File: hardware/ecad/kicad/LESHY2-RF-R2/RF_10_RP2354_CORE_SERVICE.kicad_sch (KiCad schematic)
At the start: 48 parts, among them J3 Samtec FTSH-105-01-L-DV-K-P-TR, J4 GCT USB4105-GF-A, SW1 Alps Alpine SKRTLAE010, SW2 Alps Alpine SKRTLAE010, U22 SC1512-A4, U23 Texas Instruments TPD4E05U06D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, U24 Texas Instruments TPD2EUSB30A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, U25 onsemi FSUSB42MUX, Y1 Abracon ABM8-272-T3

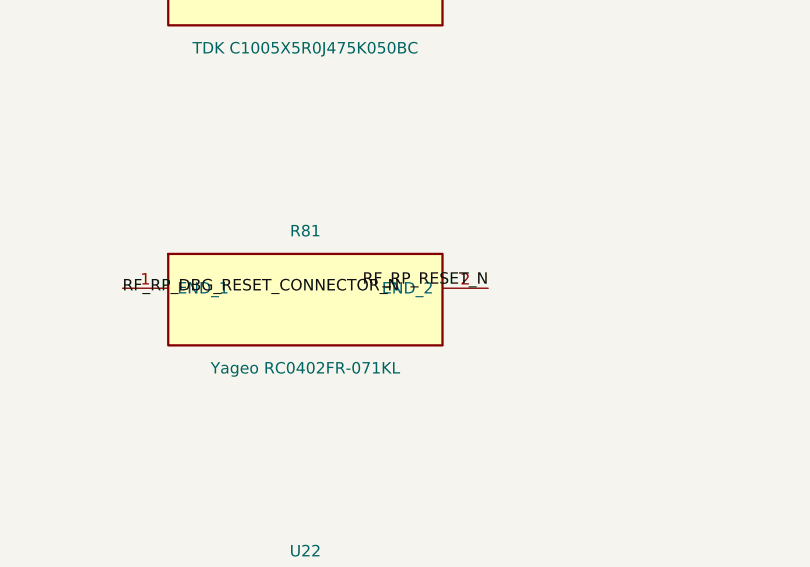
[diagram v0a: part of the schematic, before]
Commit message: Connect RF emergency reset to active RP reset net
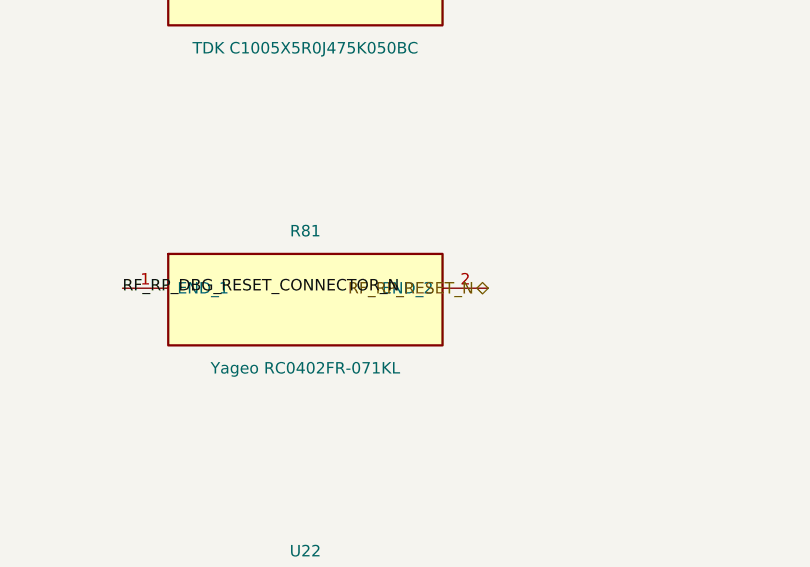
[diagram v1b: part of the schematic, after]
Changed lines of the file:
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@@
 		(effects (font (size 1.27 1.27)))
 	)
-	(label "RF_RP_RESET_N"
+	(hierarchical_label "RF_RP_RESET_N"
+		(shape bidirectional)
 		(at 716.28 121.92 180)
 		(effects (font (size 1.27 1.27)) (justify right bottom))

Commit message: Complete current R2 schematic and sourcing revalidation
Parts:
- renumbered C95 to C100, C96 to C101, C97 to C102, C98 to C103, C99 to C104, C100 to C105, C80 to C85, C81 to C86, C82 to C87, C83 to C88, C84 to C89, C85 to C90, C86 to C91, C87 to C92, C88 to C93, C89 to C94, C90 to C95, C91 to C96, C92 to C97, C93 to C98, C94 to C99, L5 to L4, R74 to R75, R75 to R76, R76 to R77, R77 to R78, R78 to R79, R79 to R80, R80 to R81, R81 to R82, R82 to R83, R83 to R84, R84 to R85, R85 to R86, R86 to R87, R87 to R88, R88 to R89, R89 to R90, R90 to R91, U22 to U23, U23 to U24, U24 to U25, U25 to U26
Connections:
- net CAP_PIN10_BUSY_OR_NFC_CS_N renamed CAP_PIN10_HOST

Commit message: Bind H6 RF and USB routing geometry
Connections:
- net RF_RP_SERVICE_USB_DM_CONNECTOR renamed RF_RP_SERVICE_USB_CONNECTOR_N
- net RF_RP_SERVICE_USB_DM_SWITCHED renamed RF_RP_SERVICE_USB_SWITCHED_N
- net RF_RP_SERVICE_USB_DP_CONNECTOR renamed RF_RP_SERVICE_USB_CONNECTOR_P
- net RF_RP_SERVICE_USB_DP_SWITCHED renamed RF_RP_SERVICE_USB_SWITCHED_P
- net RF_RP_USB_DM renamed RF_RP_USB_N
- net RF_RP_USB_DP renamed RF_RP_USB_P
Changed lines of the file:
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@@
 		(effects (font (size 1.27 1.27)))
 	)
-	(label "RF_RP_SERVICE_USB_DP_CONNECTOR"
+	(label "RF_RP_SERVICE_USB_CONNECTOR_P"
 		(at 949.96 91.44 0)
 		(effects (font (size 1.27 1.27)))
 	)
-	(label "RF_RP_SERVICE_USB_DM_CONNECTOR"
+	(label "RF_RP_SERVICE_USB_CONNECTOR_N"
 		(at 949.96 93.98 0)
 		(effects (font (size 1.27 1.27)))
@@
 		(effects (font (size 1.27 1.27)) (justify right bottom))
 	)
-	(label "RF_RP_SERVICE_USB_DP_CONNECTOR"
+	(label "RF_RP_SERVICE_USB_CONNECTOR_P"
 		(at 990.60 88.90 180)
 		(effects (font (size 1.27 1.27)) (justify right bottom))
 	)
-	(label "RF_RP_SERVICE_USB_DM_CONNECTOR"
+	(label "RF_RP_SERVICE_USB_CONNECTOR_N"
 		(at 990.60 91.44 180)
 		(effects (font (size 1.27 1.27)) (justify right bottom))
@@
 		)
 	)
-	(label "RF_RP_SERVICE_USB_DM_SWITCHED"
+	(label "RF_RP_SERVICE_USB_SWITCHED_N"
 		(at 35.56 157.48 0)
 		(effects (font (size 1.27 1.27)))
 	)
-	(label "RF_RP_USB_DM"
+	(label "RF_RP_USB_N"
 		(at 76.20 157.48 180)
 		(effects (font (size 1.27 1.27)) (justify right bottom))
@@
 		)
 	)
-	(label "RF_RP_SERVICE_USB_DP_SWITCHED"
+	(label "RF_RP_SERVICE_USB_SWITCHED_P"
 		(at 127.00 157.48 0)
 		(effects (font (size 1.27 1.27)))
 	)
-	(label "RF_RP_USB_DP"
+	(label "RF_RP_USB_P"
 		(at 167.64 157.48 180)
 		(effects (font (size 1.27 1.27)) (justify right bottom))
@@
 		(effects (font (size 1.27 1.27)) (justify right bottom))
 	)
-	(label "RF_RP_USB_DM"
+	(label "RF_RP_USB_N"
 		(at 716.28 215.90 180)
 		(effects (font (size 1.27 1.27)) (justify right bottom))
 	)
-	(label "RF_RP_USB_DP"
+	(label "RF_RP_USB_P"
 		(at 716.28 218.44 180)
 		(effects (font (size 1.27 1.27)) (justify right bottom))
@@
 		)
 	)
-	(label "RF_RP_SERVICE_USB_DP_CONNECTOR"
+	(label "RF_RP_SERVICE_USB_CONNECTOR_P"
 		(at 1041.40 157.48 0)
 		(effects (font (size 1.27 1.27)))
 	)
-	(label "RF_RP_SERVICE_USB_DM_CONNECTOR"
+	(label "RF_RP_SERVICE_USB_CONNECTOR_N"
 		(at 1041.40 160.02 0)
 		(effects (font (size 1.27 1.27)))
@@
 		(effects (font (size 1.27 1.27)))
 	)
-	(label "RF_RP_SERVICE_USB_DP_CONNECTOR"
+	(label "RF_RP_SERVICE_USB_CONNECTOR_P"
 		(at 858.52 162.56 0)
 		(effects (font (size 1.27 1.27)))
 	)
-	(label "RF_RP_SERVICE_USB_DM_CONNECTOR"
+	(label "RF_RP_SERVICE_USB_CONNECTOR_N"
 		(at 858.52 165.10 0)
 		(effects (font (size 1.27 1.27)))
@@
 		(effects (font (size 1.27 1.27)))
 	)
-	(label "RF_RP_SERVICE_USB_DM_SWITCHED"
+	(label "RF_RP_SERVICE_USB_SWITCHED_N"
 		(at 899.16 157.48 180)
 		(effects (font (size 1.27 1.27)) (justify right bottom))
 	)
-	(label "RF_RP_SERVICE_USB_DP_SWITCHED"
+	(label "RF_RP_SERVICE_USB_SWITCHED_P"
 		(at 899.16 160.02 180)
 		(effects (font (size 1.27 1.27)) (justify right bottom))

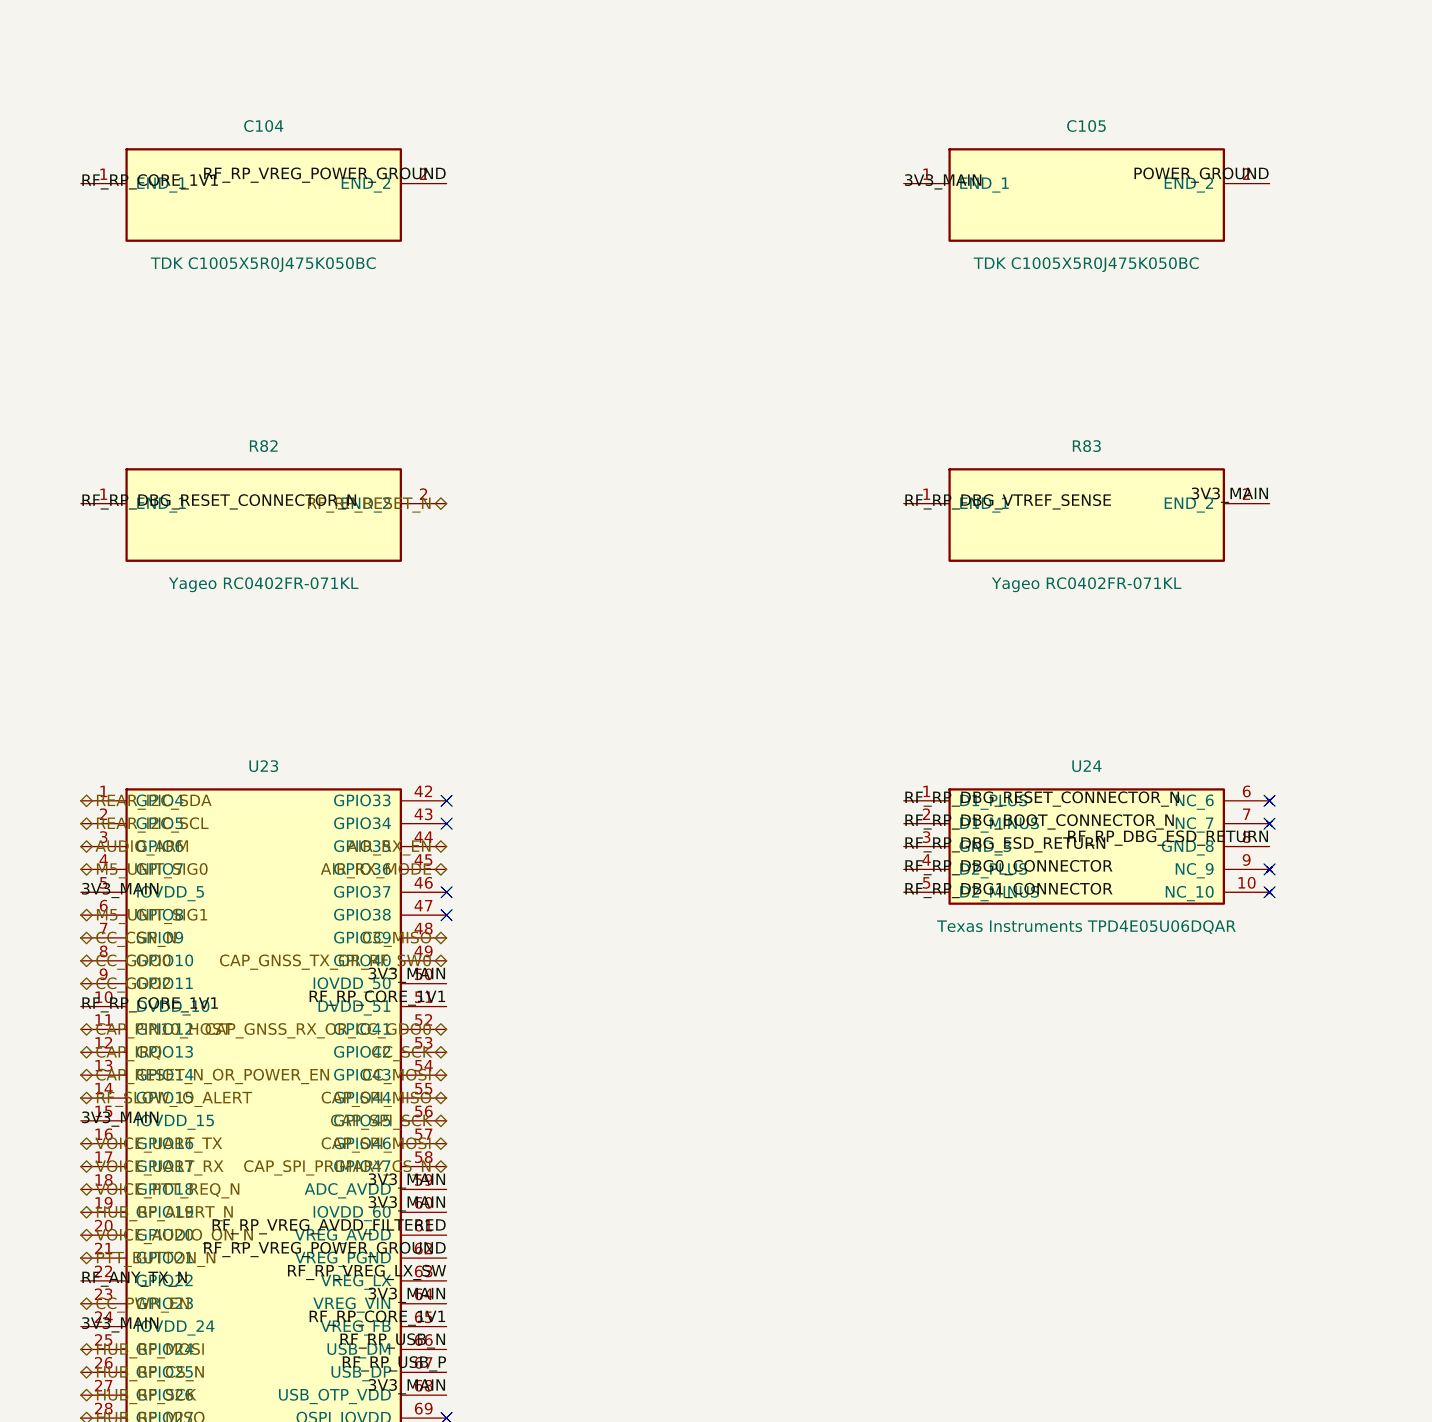
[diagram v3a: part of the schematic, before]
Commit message: Canonicalize physical ground anchors
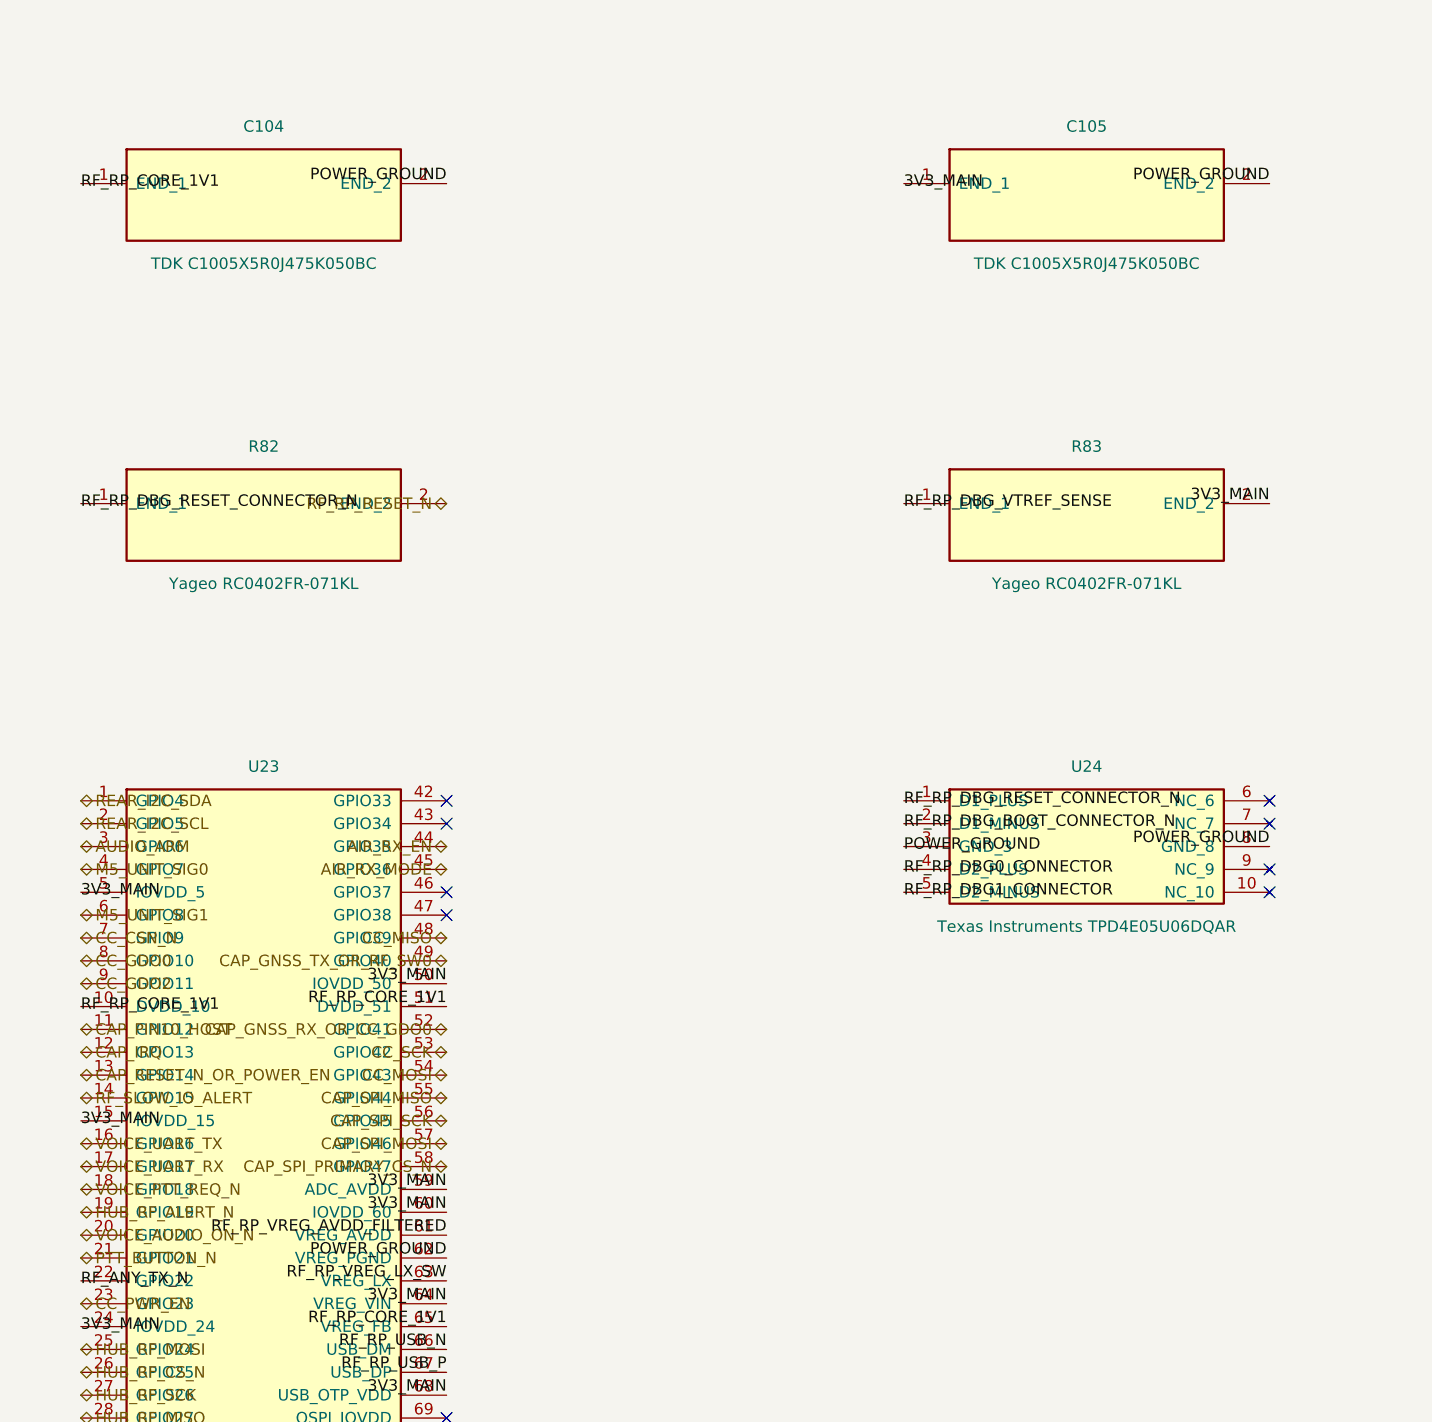
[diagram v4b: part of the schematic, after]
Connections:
- net RF_RP_DBG_ESD_RETURN is gone; now on net POWER_GROUND: U24.3 (GND_3), U24.8 (GND_8)
- net RF_RP_VREG_POWER_GROUND is gone; now on net POWER_GROUND: C104.2 (END_2), U23.62 (VREG_PGND)
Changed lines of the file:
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@@
 		(effects (font (size 1.27 1.27)))
 	)
-	(label "RF_RP_VREG_POWER_GROUND"
+	(label "POWER_GROUND"
 		(at 716.28 86.36 180)
 		(effects (font (size 1.27 1.27)) (justify right bottom))
@@
 		(effects (font (size 1.27 1.27)) (justify right bottom))
 	)
-	(label "RF_RP_VREG_POWER_GROUND"
+	(label "POWER_GROUND"
 		(at 716.28 205.74 180)
 		(effects (font (size 1.27 1.27)) (justify right bottom))
@@
 		(effects (font (size 1.27 1.27)))
 	)
-	(label "RF_RP_DBG_ESD_RETURN"
+	(label "POWER_GROUND"
 		(at 767.08 160.02 0)
 		(effects (font (size 1.27 1.27)))
@@
 	(no_connect (at 807.72 157.48)
 	)
-	(label "RF_RP_DBG_ESD_RETURN"
+	(label "POWER_GROUND"
 		(at 807.72 160.02 180)
 		(effects (font (size 1.27 1.27)) (justify right bottom))

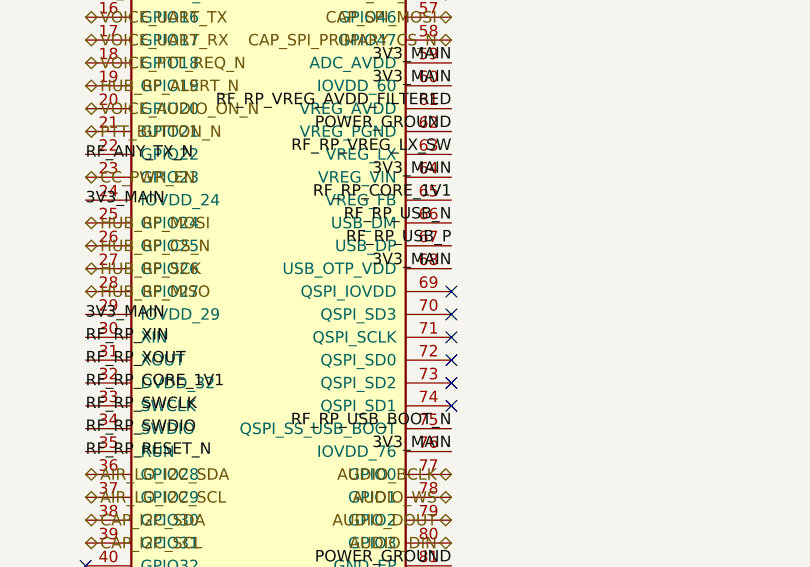
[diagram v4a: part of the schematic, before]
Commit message: Fix exact pin maps and RP flash power; add typed electrical review
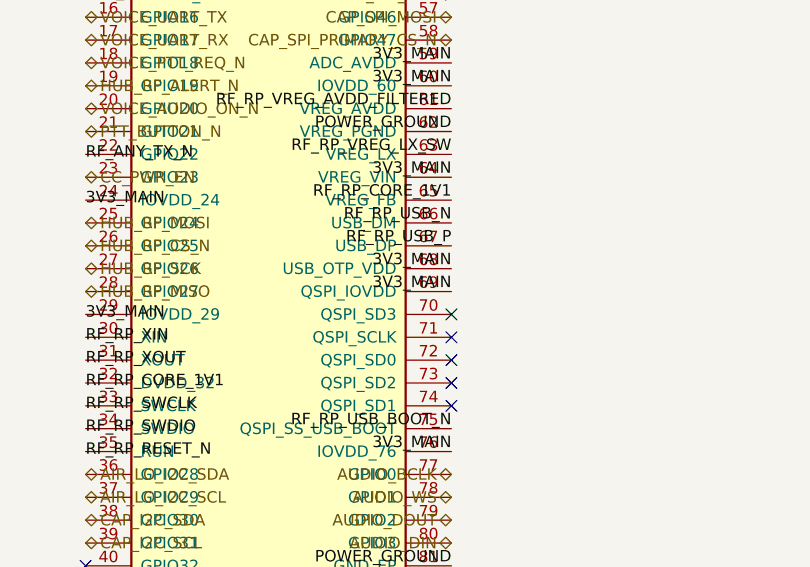
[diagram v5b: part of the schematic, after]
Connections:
- net 3V3_MAIN: now also U23.69 (QSPI_IOVDD)
- no-connect marks 19 -> 18
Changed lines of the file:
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@@
 		(effects (font (size 1.27 1.27)) (justify right bottom))
 	)
-	(no_connect (at 716.28 223.52)
+	(label "3V3_MAIN"
+		(at 716.28 223.52 180)
+		(effects (font (size 1.27 1.27)) (justify right bottom))
 	)
 	(no_connect (at 716.28 226.06)

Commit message: Correct exact connector and protection geometry; expand electrical review
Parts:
- U25: footprint Package_TO_SOT_SMD:SOT-23 -> Package_TO_SOT_SMD:Texas_DRT-3
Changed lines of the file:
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@@
 			(effects (font (size 1.27 1.27)))
 		)
-		(property "Footprint" "Package_TO_SOT_SMD:SOT-23"
+		(property "Footprint" "Package_TO_SOT_SMD:Texas_DRT-3"
 			(at 1061.72 158.75 0)
 			(show_name no)
